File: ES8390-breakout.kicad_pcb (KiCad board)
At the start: 4 copper layers, 40.5 x 60 mm, 65 parts, among them CN1 1x14_P2.54mm, CN2 PJ-327A, CN3 PJ-327A, J1 PJ-603A, J2 JST_XH_B2B, J3 JST_XH_B2B, U1 TLV9062, U2 LP5907MFX-3.0, U3 ES8390, U4 MSM381ACP003_C51928212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

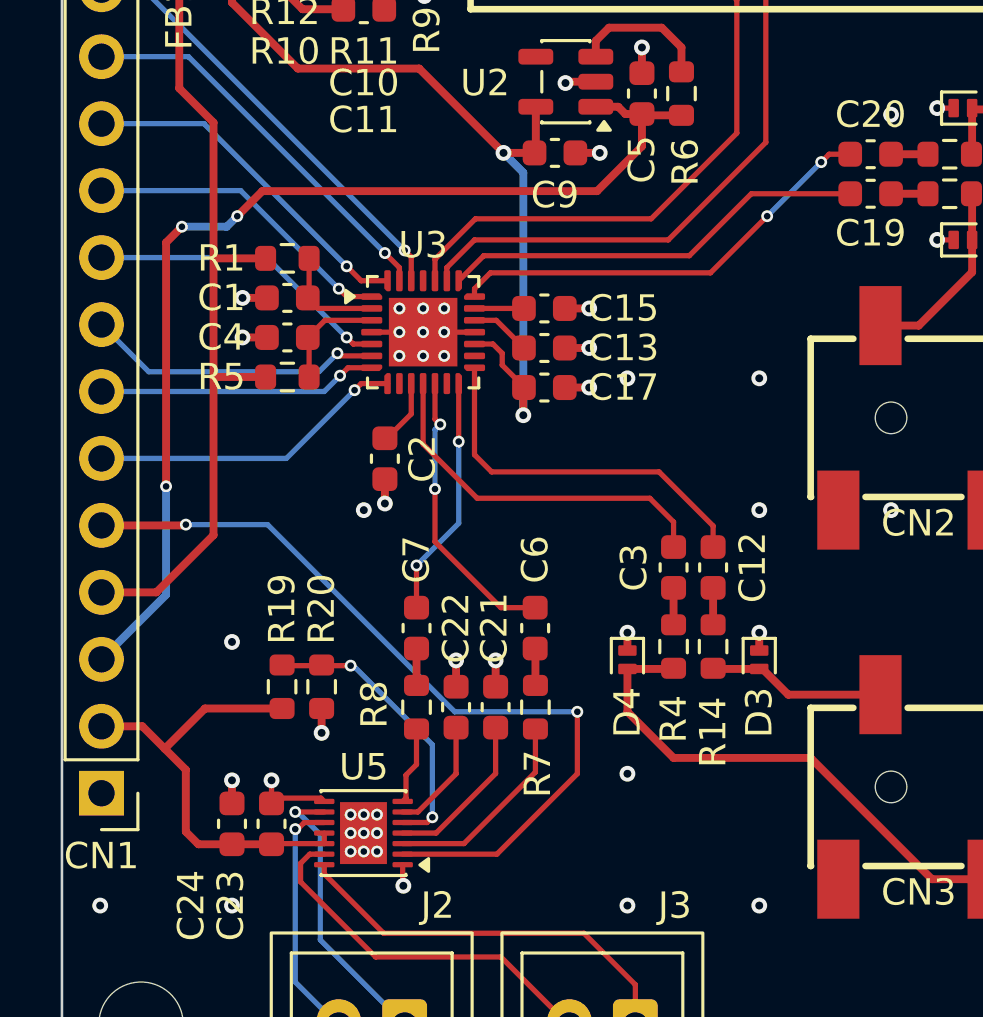
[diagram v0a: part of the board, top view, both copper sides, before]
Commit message: v0.1 ordered pcb and components
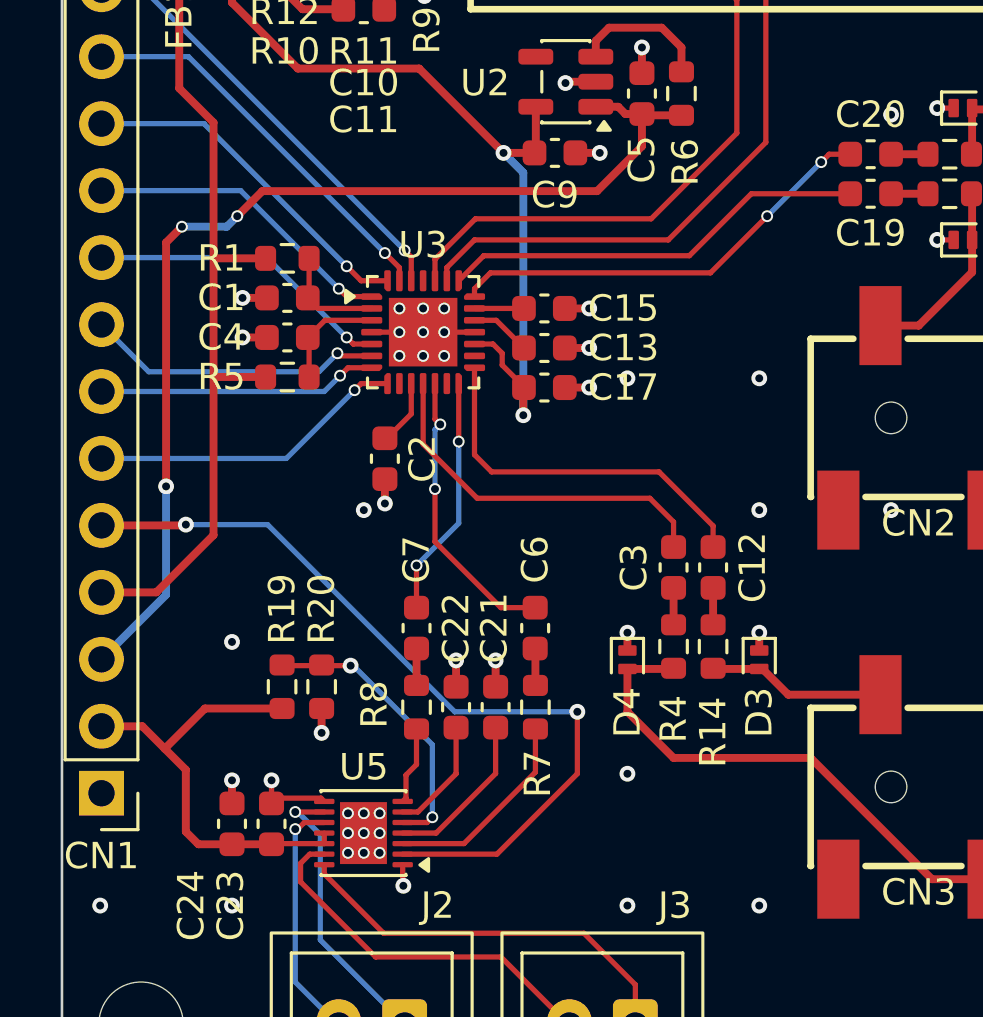
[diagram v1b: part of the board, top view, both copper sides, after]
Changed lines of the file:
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@@
 			(drillshape 0)
 			(scaleselection 1)
-			(outputdirectory "gerbers/")
+			(outputdirectory "production/gerbers/")
 		)
 	)
@@
 		(at 98.05 89.15)
 		(size 0.45)
-		(drill 0.25)
+		(drill 0.3)
 		(layers "F.Cu" "B.Cu")
 		(net "GND")
@@
 		(at 97.25 87.35)
 		(size 0.45)
-		(drill 0.25)
+		(drill 0.3)
 		(layers "F.Cu" "B.Cu")
 		(net "GND")
@@
 	)
 	(via
-		(at 94.5 107.25)
+		(at 94.4 107.25)
 		(size 0.45)
-		(drill 0.25)
+		(drill 0.3)
 		(layers "F.Cu" "B.Cu")
 		(net "GND")
@@
 		(at 97.25 89.15)
 		(size 0.45)
-		(drill 0.25)
+		(drill 0.3)
 		(layers "F.Cu" "B.Cu")
 		(net "GND")
@@
 		(at 96.35 89.15)
 		(size 0.45)
-		(drill 0.25)
+		(drill 0.3)
 		(layers "F.Cu" "B.Cu")
 		(net "GND")
@@
 	)
 	(via
-		(at 95.5 107.95)
+		(at 95.6 108)
 		(size 0.45)
-		(drill 0.25)
+		(drill 0.3)
 		(layers "F.Cu" "B.Cu")
 		(net "GND")
@@
 	)
 	(via
-		(at 95.5 107.25)
+		(at 95.6 107.25)
 		(size 0.45)
-		(drill 0.25)
+		(drill 0.3)
 		(layers "F.Cu" "B.Cu")
 		(net "GND")
@@
 		(at 98.05 88.25)
 		(size 0.45)
-		(drill 0.25)
+		(drill 0.3)
 		(layers "F.Cu" "B.Cu")
 		(net "GND")
@@
 		(at 95 107.25)
 		(size 0.45)
-		(drill 0.25)
+		(drill 0.3)
 		(layers "F.Cu" "B.Cu")
 		(net "GND")
@@
 		(at 96.35 88.25)
 		(size 0.45)
-		(drill 0.25)
+		(drill 0.3)
 		(layers "F.Cu" "B.Cu")
 		(net "GND")
@@
 	)
 	(via
-		(at 95 106.55)
+		(at 95 106.5)
 		(size 0.45)
-		(drill 0.25)
+		(drill 0.3)
 		(layers "F.Cu" "B.Cu")
 		(net "GND")
@@
 		(at 98.05 87.35)
 		(size 0.45)
-		(drill 0.25)
+		(drill 0.3)
 		(layers "F.Cu" "B.Cu")
 		(net "GND")
@@
 	)
 	(via
-		(at 95.5 106.55)
+		(at 95.6 106.5)
 		(size 0.45)
-		(drill 0.25)
+		(drill 0.3)
 		(layers "F.Cu" "B.Cu")
 		(net "GND")
@@
 		(at 97.25 88.25)
 		(size 0.45)
-		(drill 0.25)
+		(drill 0.3)
 		(layers "F.Cu" "B.Cu")
 		(net "GND")
 	)
 	(via
-		(at 95 107.95)
+		(at 95 108)
 		(size 0.45)
-		(drill 0.25)
+		(drill 0.3)
 		(layers "F.Cu" "B.Cu")
 		(net "GND")
 	)
 	(via
-		(at 94.5 107.95)
+		(at 94.4 108)
 		(size 0.45)
-		(drill 0.25)
+		(drill 0.3)
 		(layers "F.Cu" "B.Cu")
 		(net "GND")
@@
 		(at 96.35 87.35)
 		(size 0.45)
-		(drill 0.25)
+		(drill 0.3)
 		(layers "F.Cu" "B.Cu")
 		(net "GND")
@@
 	)
 	(via
-		(at 94.5 106.55)
+		(at 94.4 106.5)
 		(size 0.45)
-		(drill 0.25)
+		(drill 0.3)
 		(layers "F.Cu" "B.Cu")
 		(net "GND")
@@
 		(at 92.4 106.45)
 		(size 0.45)
-		(drill 0.25)
+		(drill 0.3)
 		(layers "F.Cu" "B.Cu")
 		(net "Net-(J3-Pin_1)")
@@
 		(at 92.4 107.100003)
 		(size 0.45)
-		(drill 0.25)
+		(drill 0.3)
 		(layers "F.Cu" "B.Cu")
 		(net "Net-(J3-Pin_2)")
@@
 		(at 90.2 83.85)
 		(size 0.45)
-		(drill 0.25)
+		(drill 0.3)
 		(layers "F.Cu" "B.Cu")
 		(net "VLDO")
@@
 		(at 88.1 84.25)
 		(size 0.45)
-		(drill 0.25)
+		(drill 0.3)
 		(layers "F.Cu" "B.Cu")
 		(net "VLDO")
@@
 	(via
 		(at 87.5 94.1)
-		(size 0.45)
-		(drill 0.25)
+		(size 0.6)
+		(drill 0.3)
 		(layers "F.Cu" "B.Cu")
 		(net "VLDO")
@@
 	(via
 		(at 94.5 100.9)
-		(size 0.45)
-		(drill 0.25)
+		(size 0.6)
+		(drill 0.3)
 		(layers "F.Cu" "B.Cu")
 		(net "Net-(U5-GAIN)")
@@
 		(at 97.6 106.65)
 		(size 0.45)
-		(drill 0.25)
+		(drill 0.3)
 		(layers "F.Cu" "B.Cu")
 		(net "Net-(U5-GAIN)")
@@
 		(at 97.9 91.75)
 		(size 0.45)
-		(drill 0.25)
+		(drill 0.3)
 		(layers "F.Cu" "B.Cu")
 		(net "Net-(U3-LOUTN)")
@@
 		(at 97.7 94.2)
 		(size 0.45)
-		(drill 0.25)
+		(drill 0.3)
 		(layers "F.Cu" "B.Cu")
 		(net "Net-(U3-LOUTN)")
@@
 	(via
 		(at 103.1 102.65)
-		(size 0.45)
-		(drill 0.25)
+		(size 0.6)
+		(drill 0.3)
 		(layers "F.Cu" "B.Cu")
 		(net "AMP_SHDN")
@@
 	(via
 		(at 88.25 95.55)
-		(size 0.45)
-		(drill 0.25)
+		(size 0.6)
+		(drill 0.3)
 		(layers "F.Cu" "B.Cu")
 		(net "AMP_SHDN")
@@
 		(at 94.65 90.45)
 		(size 0.45)
-		(drill 0.25)
+		(drill 0.3)
 		(layers "F.Cu" "B.Cu")
 		(net "ADOUT{slash}AD1")
@@
 		(at 94.1 89.9)
 		(size 0.45)
-		(drill 0.25)
+		(drill 0.3)
 		(layers "F.Cu" "B.Cu")
 		(net "LRCK")
@@
 		(at 94 89.05)
 		(size 0.45)
-		(drill 0.25)
+		(drill 0.3)
 		(layers "F.Cu" "B.Cu")
 		(net "DSDIN")
@@
 		(at 94.35 88.45)
 		(size 0.45)
-		(drill 0.25)
+		(drill 0.3)
 		(layers "F.Cu" "B.Cu")
 		(net "SCLK")
@@
 		(at 94.05 86.6)
 		(size 0.45)
-		(drill 0.25)
+		(drill 0.3)
 		(layers "F.Cu" "B.Cu")
 		(net "MCLK")
@@
 		(at 94.35 85.75)
 		(size 0.45)
-		(drill 0.25)
+		(drill 0.3)
 		(layers "F.Cu" "B.Cu")
 		(net "CCLK")
@@
 		(at 95.8 85.25)
 		(size 0.45)
-		(drill 0.25)
+		(drill 0.3)
 		(layers "F.Cu" "B.Cu")
 		(net "CDATA")
@@
 		(at 96.55 85.15)
 		(size 0.45)
-		(drill 0.25)
+		(drill 0.3)
 		(layers "F.Cu" "B.Cu")
 		(net "AD0{slash}DMIC_SCL")
@@
 		(at 112.35 81.8)
 		(size 0.45)
-		(drill 0.25)
+		(drill 0.3)
 		(layers "F.Cu" "B.Cu")
 		(net "Net-(U3-RIN2)")
@@
 		(at 110.3 83.85)
 		(size 0.45)
-		(drill 0.25)
+		(drill 0.3)
 		(layers "F.Cu" "B.Cu")
 		(net "Net-(U3-RIN2)")
@@
 		(at 98.6 92.4)
 		(size 0.45)
-		(drill 0.25)
+		(drill 0.3)
 		(layers "F.Cu" "B.Cu")
 		(net "Net-(U3-ROUTN)")
@@
 		(at 97 97.1)
 		(size 0.45)
-		(drill 0.25)
+		(drill 0.3)
 		(layers "F.Cu" "B.Cu")
 		(net "Net-(U3-ROUTN)")
